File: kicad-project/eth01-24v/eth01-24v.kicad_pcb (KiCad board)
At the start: 2 copper layers, 4 parts, among them U1 WT32-ETH01, U2 XL-6009-ADJ

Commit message: ajout photos et première version pcb
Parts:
- added BSS1: ~, WT32-ETH01:BSS138, F.Cu at (175.4, 89.6)
- added J1: KF301-2P, WT32-ETH01:KF3012P, F.Cu at (82.5, 148.5)
- added J10: KF301-2P, WT32-ETH01:KF3012P, F.Cu at (97.5, 71.2)
- added J11: KF301-2P, WT32-ETH01:KF3012P, F.Cu at (92.5, 148.5)
- added J12: KF301-2P, WT32-ETH01:KF3012P, F.Cu at (150.5, 71.5)
- added J13: KF301-3P, WT32-ETH01:KF3013P, F.Cu at (180.5, 71.5)
- added J2: KF301-3P, WT32-ETH01:KF3013P, F.Cu at (147.5, 148.5)
- added J3: KF301-3P, WT32-ETH01:KF3013P, F.Cu at (132.5, 148.5)
- added J4: KF301-3P, WT32-ETH01:KF3013P, F.Cu at (162.5, 148.5)
- added J5: KF301-3P, WT32-ETH01:KF3013P, F.Cu at (117.5, 148.5)
- added J6: KF301-3P, WT32-ETH01:KF3013P, F.Cu at (102.5, 148.5)
- added J7: KF301-3P, WT32-ETH01:KF3013P, F.Cu at (112.5, 71.2)
- added J8: KF301-3P, WT32-ETH01:KF3013P, F.Cu at (165.5, 71.5)
- added J9: KF301-2P, WT32-ETH01:KF3012P, F.Cu at (87.5, 71.2)
- added U5: ~, WT32-ETH01:OP71A04, F.Cu at (79.1, 109.5)
- added U7: ~, WT32-ETH01:OP71A04, F.Cu at (79.1, 88.0)
- added U8: ~, WT32-ETH01:MP1584_AIO, F.Cu at (175.6, 108.9)
- U2: value XL-6009-ADJ -> ~; footprint esp32-24v-io:XL6009_module_SMT -> WT32-ETH01:MCP23017
- moved U4 140.8 mm to (79.1, 131.0), turned to 0 degrees
- moved U3 53.6 mm to (145.6, 131.0), turned to 0 degrees
- moved U2 31.6 mm to (156.2, 96.1)
- moved U1 23.7 mm to (132.2, 105.1), turned to 180 degrees
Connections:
- U1 pad 10: Net-(U4-Vcc) -> 3.3V
- U1 pad 12: Net-(U1-5V) -> 5V
- U1 pad 16: unconnected-(U1-IO4/ADC2_CH0/TCH0-Pad16) -> Net-(BSS1-LV3)
- U1 pad 19: Net-(U1-IO14/ADC2_CH6/TCH6) -> Net-(BSS1-LV2)
- U1 pad 20: Net-(U1-IO15/ADC2_CH3/TCH3) -> Net-(BSS1-LV1)
- U1 pad 21: Net-(U1-IO36/ADC1_CH0/INPUT_ONLY) -> /InterruptA
- U1 pad 22: Net-(U1-IO39/ADC1_CH3/INPUT_ONLY) -> /InteruptB
- U1 pad 23: unconnected-(U1-GND-Pad23) -> GND
- U1 pad 3: Net-(U4-Vcc) -> 3.3V
- U1 pad 5: Net-(U1-IO32/ADC1_CH4/TCH9) -> /SCL
- U1 pad 6: Net-(U1-IO33/ADC1_CH5/TCH8) -> /SDA
- U1 pad 7: Net-(U1-IO5/BOOT_FLOAT) -> unconnected-(U1-IO5/BOOT_FLOAT-Pad7)
- U1 pad 8: Net-(U1-IO17/UART2_TX) -> unconnected-(U1-IO17/UART2_TX-Pad8)
- U2 pad 1: +24V -> unconnected-(U2-A2-Pad1)
- U2 pad 2: GND -> unconnected-(U2-A1-Pad2)
- U2 pad 3: Net-(U1-5V) -> unconnected-(U2-A0-Pad3)
- U2 pad 4: GND -> unconnected-(U2-RESET-Pad4)
- U3 pad 1: Net-(U1-IO32/ADC1_CH4/TCH9) -> Net-(U3-1+)
- U3 pad 11: OUT1 -> Net-(U2-B3)
- U3 pad 12: OUT2 -> Net-(U2-B2)
- U3 pad 13: OUT3 -> Net-(U2-B1)
- U3 pad 14: OUT4 -> Net-(U2-B0)
- U3 pad 3: Net-(U1-IO33/ADC1_CH5/TCH8) -> Net-(U3-2+)
- U3 pad 5: Net-(U1-IO5/BOOT_FLOAT) -> Net-(U3-3+)
- U3 pad 7: Net-(U1-IO17/UART2_TX) -> Net-(U3-4+)
- U3 pad 9: +24V -> 3.3V
- U4 pad 1: IN1-24V -> /E-STOP
- U4 pad 11: Net-(U1-IO39/ADC1_CH3/INPUT_ONLY) -> Net-(U2-B7)
- U4 pad 12: Net-(U1-IO36/ADC1_CH0/INPUT_ONLY) -> Net-(U2-B6)
- U4 pad 13: Net-(U1-IO15/ADC2_CH3/TCH3) -> Net-(U2-B5)
- U4 pad 14: Net-(U1-IO14/ADC2_CH6/TCH6) -> Net-(U2-B4)
- U4 pad 3: IN2-24V -> /SIGNAL
- U4 pad 5: IN3-24V -> Net-(U4-3+)
- U4 pad 7: IN4-24V -> Net-(U4-4+)
- U4 pad 9: Net-(U4-Vcc) -> 3.3V
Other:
- board outline added: 107 x 87 mm
- board text added: "+24V"
- board text added: "DIR+"
- board text added: "DIR-"
- board text added: "EN+"
- board text added: "EN-"
- board text added: "GND"
- board text added: "MOTOR DRIVER"
- board text added: "PUL+"
- board text added: "PUL-"

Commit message: routage ok
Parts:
- added DRA1: DIN_Rail_Adapter, MountingEquipment:DINRailAdapter_3xM3_PhoenixContact_1201578, F.Cu at (155.5, 106.0)
- added DRA2: DIN_Rail_Adapter, MountingEquipment:DINRailAdapter_3xM3_PhoenixContact_1201578, F.Cu at (93.5, 106.0)
- J2: value KF301-3P -> KF301-2P; footprint WT32-ETH01:KF3013P -> WT32-ETH01:KF3012P
- U3, U4: footprint WT32-ETH01:OP71A04 -> WT32-ETH01:OP71A04 - 24V3.3V
- U5, U7: footprint WT32-ETH01:OP71A04 -> WT32-ETH01:OP71A04 - 3.3V24V
- moved J1 93.0 mm to (175.5, 148.1)
- moved J7 79.5 mm to (133.0, 148.1), turned to 0 degrees
- moved J11 78.6 mm to (107.7, 71.4), turned to 180 degrees
- moved U7 57.4 mm to (117.9, 130.3), turned to 180 degrees
- moved J4 44.5 mm to (118.0, 148.1)
- moved U4 43.4 mm to (78.9, 87.6)
- moved U5 38.8 mm to (117.9, 109.0), turned to 180 degrees
- moved J2 15.6 mm to (163.1, 148.1)
- moved J3 15.5 mm to (148.0, 148.1)
- moved J5 14.5 mm to (103.0, 148.1)
- moved J6 14.5 mm to (88.0, 148.1)
- moved U3 1.23 mm to (145.0, 132.1)
- moved U1 0.79 mm to (131.4, 105.5)
- moved U2 0.72 mm to (155.4, 96.3), turned to 180 degrees
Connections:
- BSS1 pad 9: +5V -> 5V
- J1 pad 2: +24V -> GND
- J11 pad 1: Net-(J11-Pad1) -> +24V
- J11 pad 2: Net-(J11-Pad1) -> GND
- J2 pad 2: /SIGNAL -> GND
- U8 pad 1: +24V -> GND
- U8 pad 2: +24V -> GND
- U8 pad 3: Net-(J11-Pad1) -> +24V
- U8 pad 4: Net-(J11-Pad1) -> +24V
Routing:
- net +24V: track 0.00 -> 262.8 mm
- net 3.3V: track 0.00 -> 164.7 mm, vias 0 -> 3
- net Net-(U4-3+): track 0.00 -> 118.2 mm
- net Net-(BSS1-LV3): track 0.00 -> 114.4 mm
- net Net-(U4-4+): track 0.00 -> 114.1 mm
- net Net-(BSS1-LV2): track 0.00 -> 101.5 mm
- net Net-(BSS1-LV1): track 0.00 -> 96.0 mm
- net GND: track 0.00 -> 90.9 mm
- net 5V: track 0.00 -> 81.7 mm
- net Net-(U2-A5): track 0.00 -> 76.8 mm, vias 0 -> 1
- net Net-(U2-A6): track 0.00 -> 72.3 mm
- net Net-(U2-A7): track 0.00 -> 68.4 mm
- net Net-(U2-A4): track 0.00 -> 65.2 mm, vias 0 -> 1
- net Net-(U2-B4): track 0.00 -> 63.2 mm
- net Net-(U2-B5): track 0.00 -> 56.5 mm
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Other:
- board text added: "24V"
- board text added: "A0"
- board text added: "A1"
- board text added: "A2"
- board text added: "A3"
- board text added: "A4"
- board text added: "A5"
- board text added: "A6"
- board text added: "A7"
- board text added: "B0"
- board text added: "B1"
- board text added: "B2"
- board text added: "B3"
- board text added: "B4"
- board text added: "B5"
- board text added: "E-STOP"
- board text added: "OUTPUTS"
- board text added: "SIGNAL"
- board text added: "SONDE Z"

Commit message: plan masse
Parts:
- moved J11 0.21 mm to (107.5, 71.3)
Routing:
- net GND: track 90.9 -> 125.7 mm, vias 0 -> 1
- net +24V: track 262.8 -> 257.6 mm
- added copper zone on B.Cu, net GND
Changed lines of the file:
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@@
 	(footprint "WT32-ETH01:KF3012P"
 		(layer "F.Cu")
-		(at 107.696 71.374 180)
+		(at 107.529 71.251 180)
 		(descr "KF301-2P-1")
 		(tags "Connector")
@@
 	)
 	(segment
+		(start 176.706 94.66)
+		(end 176.706 84.754)
+		(width 1)
+		(layer "F.Cu")
+		(net 1)
+	)
+	(segment
+		(start 164.338 87.376)
+		(end 157.226 87.376)
+		(width 1)
+		(layer "F.Cu")
+		(net 1)
+	)
+	(segment
+		(start 176.706 84.754)
+		(end 176.96 84.5)
+		(width 1)
+		(layer "F.Cu")
+		(net 1)
+	)
+	(segment
+		(start 145.542 123.19)
+		(end 145.542 125.476)
+		(width 1)
+		(layer "F.Cu")
+		(net 1)
+	)
+	(segment
+		(start 142.86 121.96)
+		(end 144.312 121.96)
+		(width 1)
+		(layer "F.Cu")
+		(net 1)
+	)
+	(segment
+		(start 176.706 96.727)
+		(end 179.628 99.649)
+		(width 1)
+		(layer "F.Cu")
+		(net 1)
+	)
+	(segment
+		(start 145.796 125.73)
+		(end 148.59 125.73)
+		(width 1)
+		(layer "F.Cu")
+		(net 1)
+	)
+	(segment
+		(start 176.706 94.66)
+		(end 176.706 96.727)
+		(width 1)
+		(layer "F.Cu")
+		(net 1)
+	)
+	(segment
+		(start 144.312 121.96)
+		(end 145.542 123.19)
+		(width 1)
+		(layer "F.Cu")
+		(net 1)
+	)
+	(segment
+		(start 145.542 125.476)
+		(end 145.796 125.73)
+		(width 1)
+		(layer "F.Cu")
+		(net 1)
+	)
+	(segment
+		(start 182.168 99.649)
+		(end 179.628 99.649)
+		(width 1)
+		(layer "F.Cu")
+		(net 1)
+	)
+	(via
+		(at 157.226 87.376)
+		(size 0.6)
+		(drill 0.3)
+		(layers "F.Cu" "B.Cu")
+		(net 1)
+	)
+	(segment
 		(start 102.696 76.788)
 		(end 109.728 83.82)
@@
 	)
 	(segment
-		(start 107.696 71.374)
-		(end 107.696 73.152)
-		(width 1.5)
-		(layer "F.Cu")
-		(net 60)
-	)
-	(segment
 		(start 79.502 101.854)
 		(end 82.296 99.06)
@@
 	)
 	(segment
-		(start 182.168 99.649)
-		(end 179.628 99.649)
-		(width 1)
-		(layer "F.Cu")
-		(net 60)
-	)
-	(segment
 		(start 183.642 122.428)
 		(end 179.324 122.428)
@@
 	)
 	(segment
+		(start 107.442 73.406)
+		(end 106.172 74.676)
+		(width 1.5)
+		(layer "F.Cu")
+		(net 60)
+	)
+	(segment
 		(start 88.9 73.914)
 		(end 89.662 74.676)
@@
 	(segment
 		(start 145.5 71.5)
-		(end 154.01 80.01)
+		(end 148.676 74.676)
+		(width 1)
+		(layer "F.Cu")
+		(net 60)
+	)
+	(segment
+		(start 142.324 74.676)
+		(end 148.676 74.676)
 		(width 1)
 		(layer "F.Cu")
@@
 	)
 	(segment
+		(start 107.442 71.164)
+		(end 107.442 73.406)
+		(width 1.5)
+		(layer "F.Cu")
+		(net 60)
+	)
+	(segment
 		(start 180.086 144.272)
 		(end 183.642 140.716)
@@
 	)
 	(segment
-		(start 107.696 73.152)
-		(end 106.172 74.676)
-		(width 1.5)
-		(layer "F.Cu")
-		(net 60)
-	)
-	(segment
 		(start 82.296 99.06)
 		(end 84.074 99.06)
@@
 	)
 	(segment
+		(start 148.676 74.676)
+		(end 154.01 80.01)
+		(width 1)
+		(layer "F.Cu")
+		(net 60)
+	)
+	(segment
 		(start 82.1255 115.316)
 		(end 80.772 115.316)
@@
 	)
 	(segment
+		(start 107.529 71.251)
+		(end 107.442 71.164)
+		(width 1.5)
+		(layer "F.Cu")
+		(net 60)
+	)
+	(segment
 		(start 168.402 97.028)
 		(end 171.45 97.028)
@@
 	)
 	(segment
-		(start 171.45 97.028)
-		(end 177.007 97.028)
-		(width 1)
-		(layer "F.Cu")
-		(net 60)
-	)
-	(segment
-		(start 177.007 97.028)
-		(end 179.628 99.649)
-		(width 1)
-		(layer "F.Cu")
-		(net 60)
-	)
-	(segment
 		(start 183.642 140.716)
 		(end 183.642 122.428)
@@
 		(net 65)
 	)
+	(zone
+		(net 1)
+		(net_name "GND")
+		(layer "B.Cu")
+		(name "MASSE")
+		(hatch edge 0.5)
+		(connect_pads
+			(clearance 0.5)
+		)
+		(min_thickness 0.25)
+		(filled_areas_thickness no)
+		(fill yes
+			(thermal_gap 0.5)
+			(thermal_bridge_width 0.5)
+		)
+		(polygon
+			(pts
+				(xy 77.724 152.908) (xy 184.658 153.162) (xy 184.658 66.04) (xy 77.978 66.04) (xy 77.978 71.374)
+			)
+		)
+	)
 	(embedded_fonts no)

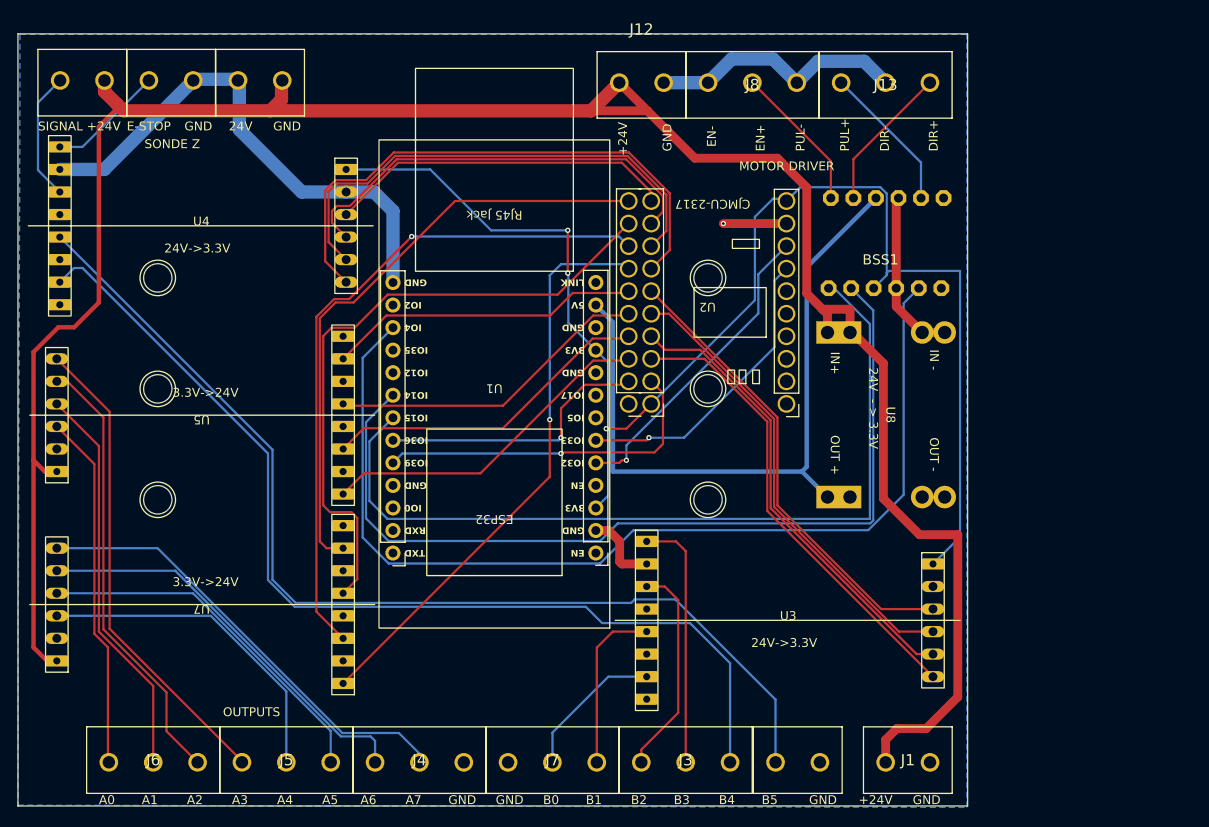
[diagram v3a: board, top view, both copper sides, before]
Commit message: routage ok - silk screen corrigé- impression
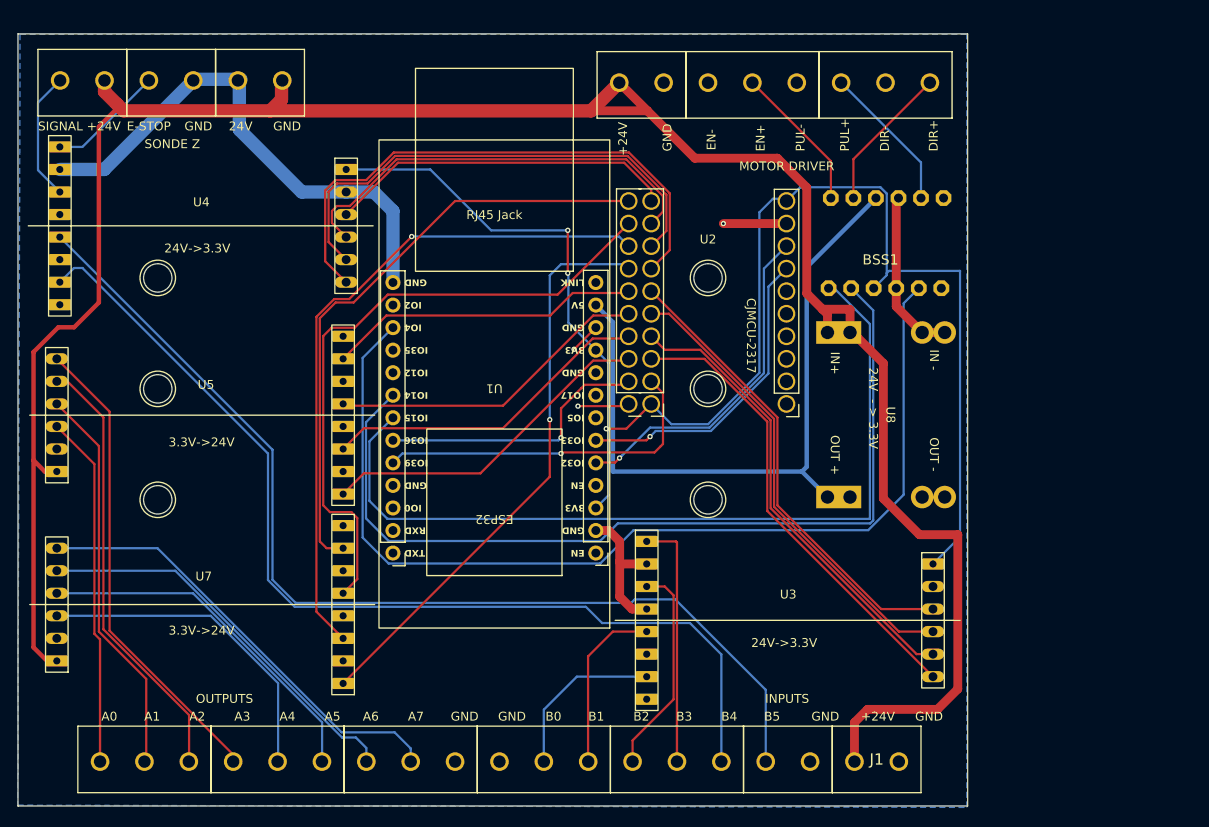
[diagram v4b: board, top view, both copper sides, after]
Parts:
- moved J1 3.51 mm to (172.0, 148.0)
- moved J2 1.11 mm to (162.0, 148.0)
- moved J5 0.99 mm to (102.0, 148.0)
- moved J6 0.99 mm to (87.0, 148.0)
- moved J3 0.99 mm to (147.0, 148.0)
- moved J4 0.99 mm to (117.0, 148.0)
- moved J7 0.97 mm to (132.0, 148.0)
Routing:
- net GND: track 125.7 -> 113.3 mm, vias 1 -> 3
- net 3.3V: track 164.7 -> 171.7 mm
- net +24V: track 257.6 -> 261.7 mm
- net /SCL: track 35.2 -> 38.8 mm
- net Net-(U3-4+): track 16.6 -> 19.0 mm
- net Net-(U3-1+): track 28.6 -> 27.3 mm
- net /SDA: track 33.9 -> 35.2 mm
- net Net-(U7-O4): track 51.4 -> 50.7 mm
- net Net-(U7-O3): track 46.2 -> 45.6 mm
- net Net-(U4-3+): track 118.2 -> 117.7 mm
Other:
- board text added: "INPUTS"
